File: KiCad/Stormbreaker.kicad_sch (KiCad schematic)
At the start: 42 parts, among them J1 Micro_SD_Card_Det2, J2 USB_C_Receptacle_USB2.0_14P, J3 Conn_01x03, Q1 PMOS, SW1 SW_Push, U1 BQ25895RTW, U3 ATtiny1616-M

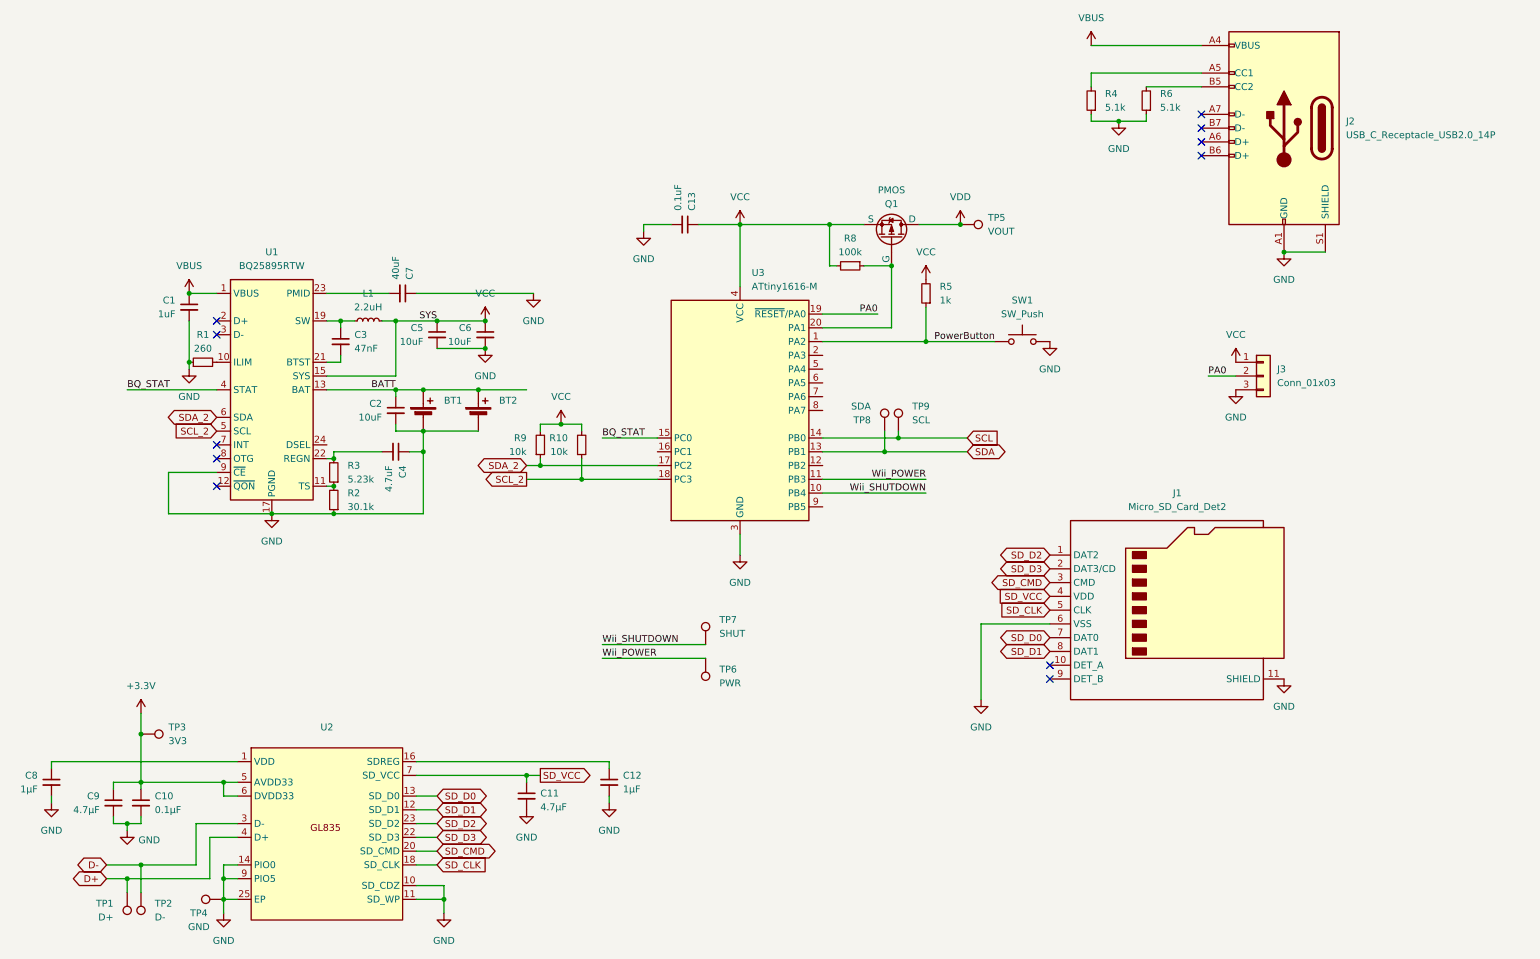
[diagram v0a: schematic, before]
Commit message: Added fan and other batt, via stitched
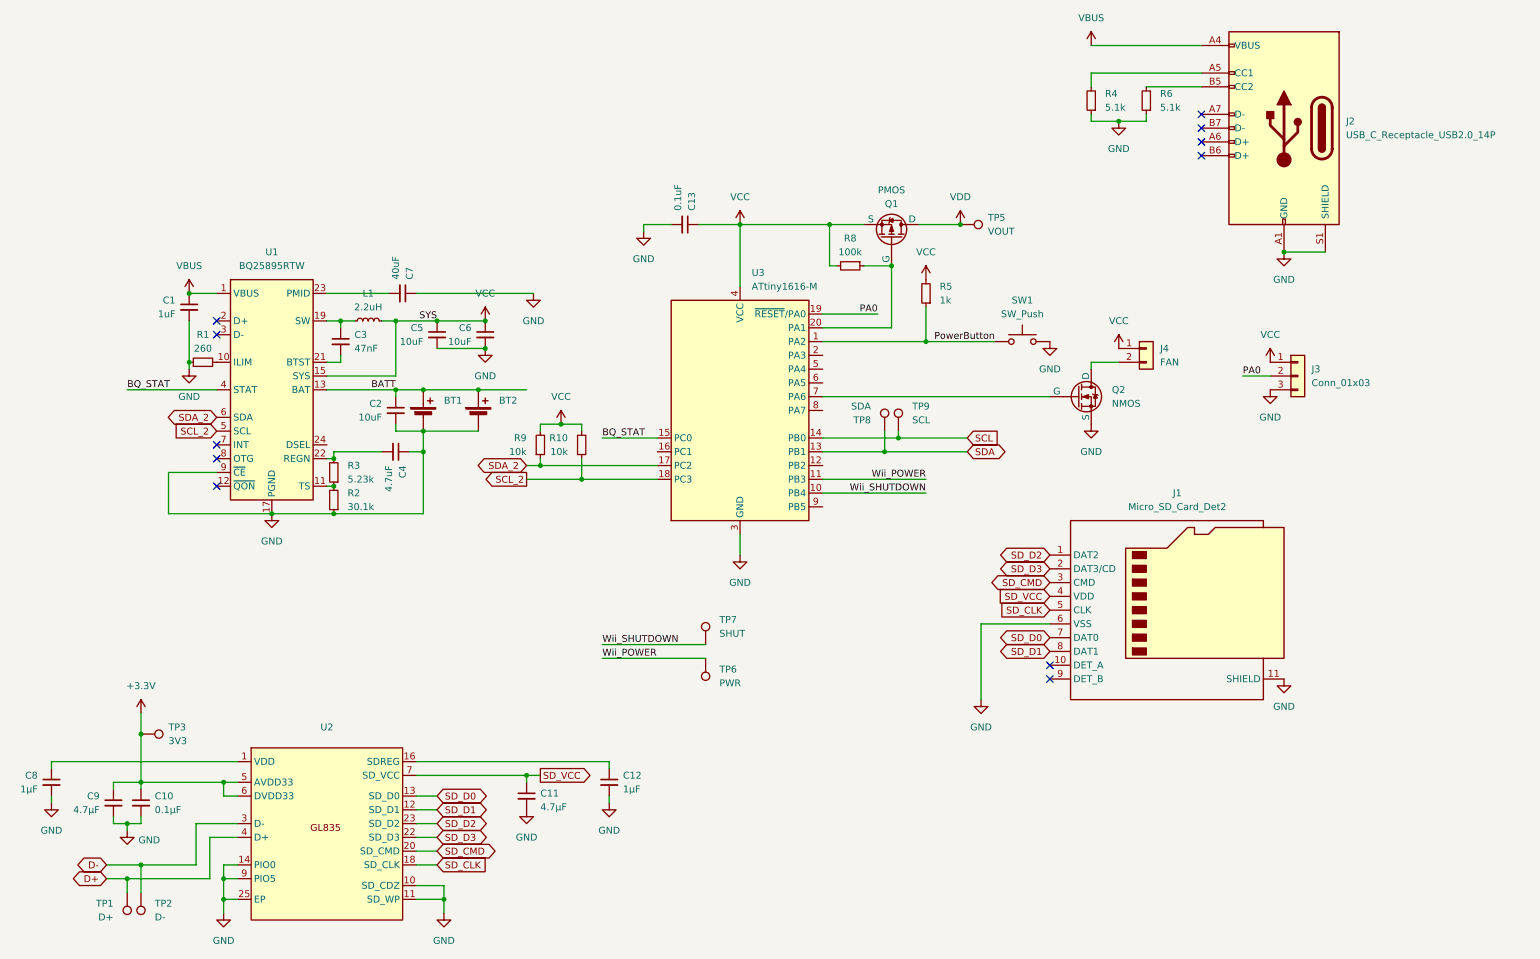
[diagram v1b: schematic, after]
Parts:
- removed TP4: GND, TestPoint:TestPoint_Pad_D3.0mm, symbol Connector:TestPoint
- added J4: FAN, Connector_PinSocket_1.00mm:PinSocket_1x02_P1.00mm_Vertical, symbol Connector_Generic:Conn_01x02
- added Q2: NMOS, Package_TO_SOT_SMD:SOT-23-3, symbol Simulation_SPICE:NMOS
- BT1: footprint Connector_JST:JST_PH_B2B-PH-K_1x02_P2.00mm_Vertical -> Connector_PinSocket_1.27mm:PinSocket_1x02_P1.27mm_Vertical
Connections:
- net GND: now also Q2.2 (S)
- net VCC: now also J4.1 (Pin_1)
- net at U3.7 (PA6): now also Q2.1 (G)
- new net: J4.2 (Pin_2), Q2.3 (D)
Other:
- moved on the sheet: J3

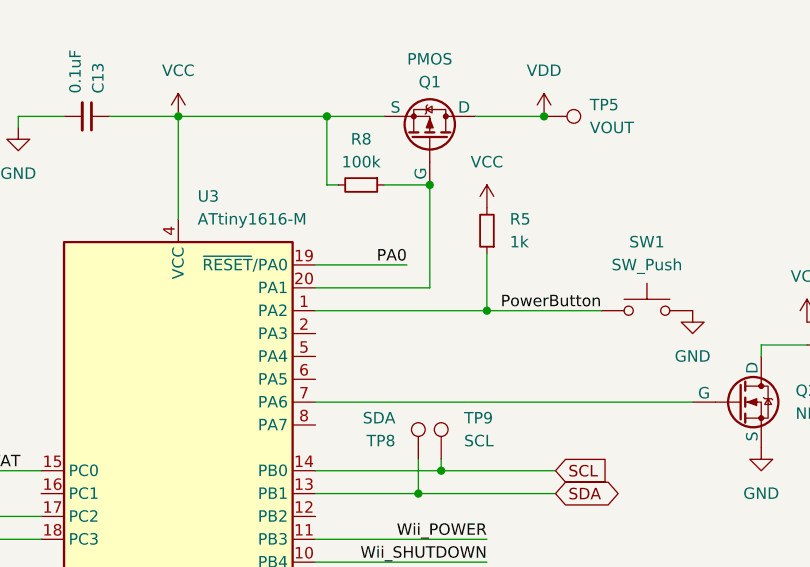
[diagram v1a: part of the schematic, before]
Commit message: Add point for neopixel
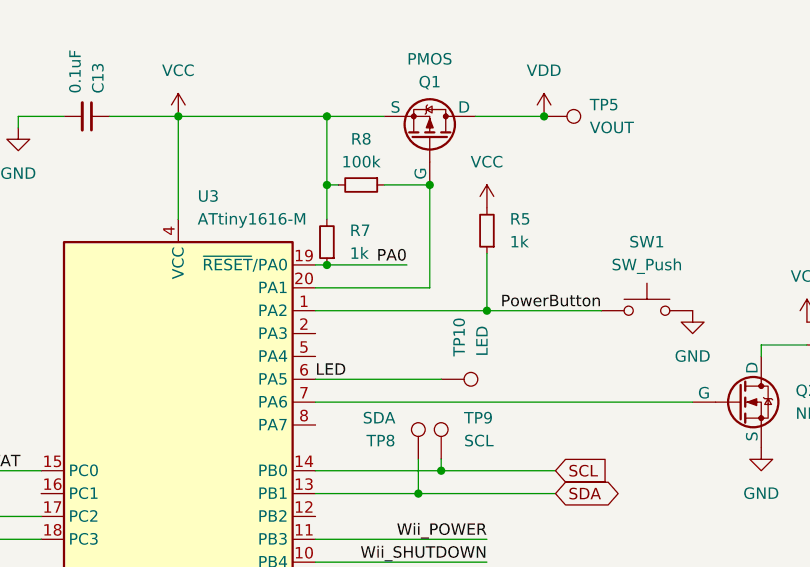
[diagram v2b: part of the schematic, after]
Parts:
- added R7: 1k, Resistor_SMD:R_0603_1608Metric, symbol Device:R_Small
- added TP10: LED, TestPoint:TestPoint_Pad_D1.0mm, symbol Connector:TestPoint
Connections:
- net PA0: now also R7.1
- net VCC: now also R7.2
- net LED: now reaches U3.6 (PA5)
- net LED: now also TP10.1
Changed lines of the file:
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@@
+	)
+	(junction
+		(at 189.23 60.96)
+		(diameter 0)
+		(color 0 0 0 0)
+	)
+	(junction
+		(at 189.23 69.85)
+		(diameter 0)
+		(color 0 0 0 0)
 	)
 	(junction
@@
 	(wire
 		(pts
-			(xy 187.96 69.85) (xy 198.12 69.85)
+			(xy 187.96 69.85) (xy 189.23 69.85)
 		)
 		(stroke
@@
 	(wire
 		(pts
+			(xy 189.23 69.85) (xy 198.12 69.85)
+		)
+		(stroke
+			(width 0)
+			(type default)
+		)
+	)
+	(wire
+		(pts
 			(xy 77.47 171.45) (xy 77.47 173.99)
 		)
@@
 	(wire
 		(pts
+			(xy 189.23 60.96) (xy 189.23 64.77)
+		)
+		(stroke
+			(width 0)
+			(type default)
+		)
+	)
+	(wire
+		(pts
 			(xy 135.89 97.79) (xy 157.48 97.79)
 		)
@@
 	(wire
 		(pts
+			(xy 187.96 82.55) (xy 201.93 82.55)
+		)
+		(stroke
+			(width 0)
+			(type default)
+		)
+	)
+	(wire
+		(pts
 			(xy 59.69 173.99) (xy 74.93 173.99)
 		)
@@
 			(width 0)
 			(type default)
+		)
+	)
+	(label "LED"
+		(at 187.96 82.55 0)
+		(effects
+			(font
+				(size 1.27 1.27)
+			)
+			(justify left bottom)
 		)
 	)
@@
 	)
 	(symbol
+		(lib_id "Device:R_Small")
+		(at 189.23 67.31 180)
+		(unit 1)
+		(exclude_from_sim no)
+		(in_bom yes)
+		(on_board yes)
+		(dnp no)
+		(fields_autoplaced yes)
+		(property "Reference" "R7"
+			(at 191.77 66.0399 0)
+			(effects
+				(font
+					(size 1.27 1.27)
+				)
+				(justify right)
+			)
+		)
+		(property "Value" "1k"
+			(at 191.77 68.5799 0)
+			(effects
+				(font
+					(size 1.27 1.27)
+				)
+				(justify right)
+			)
+		)
+		(property "Footprint" "Resistor_SMD:R_0603_1608Metric"
+			(at 189.23 67.31 0)
+			(effects
+				(font
+					(size 1.27 1.27)
+				)
+				(hide yes)
+			)
+		)
+		(property "Datasheet" "~"
+			(at 189.23 67.31 0)
+			(effects
+				(font
+					(size 1.27 1.27)
+				)
+				(hide yes)
+			)
+		)
+		(property "Description" "Resistor, small symbol"
+			(at 189.23 67.31 0)
+			(effects
+				(font
+					(size 1.27 1.27)
+				)
+				(hide yes)
+			)
+		)
+		(pin "2"
+		)
+		(pin "1"
+		)
+		(instances
+			(project "Stormbreaker"
+				(path "/dcc89f95-4ae4-4756-aa81-33bf4d3c86ca"
+					(reference "R7")
+					(unit 1)
+				)
+			)
+		)
+	)
+	(symbol
 		(lib_id "power:GND")
 		(at 172.72 114.3 0)
@@
 					(unit 1)
 				)
+			)
+		)
+	)
+	(symbol
+		(lib_id "Connector:TestPoint")
+		(at 201.93 82.55 270)
+		(unit 1)
+		(exclude_from_sim no)
+		(in_bom yes)
+		(on_board yes)
+		(dnp no)
+		(property "Reference" "TP10"
+			(at 203.9619 80.01 0)
+			(effects
+				(font
+					(size 1.27 1.27)
+				)
+				(justify right)
+			)
+		)
+		(property "Value" "LED"
+			(at 206.5019 80.01 0)
+			(effects
+				(font
+					(size 1.27 1.27)
+				)
+				(justify right)
+			)
+		)
+		(property "Footprint" "TestPoint:TestPoint_Pad_D1.0mm"
+			(at 201.93 87.63 0)
+			(effects
+				(font
+					(size 1.27 1.27)
+				)
+				(hide yes)
+			)
+		)
+		(property "Datasheet" "~"
+			(at 201.93 87.63 0)
+			(effects
+				(font
+					(size 1.27 1.27)
+				)
+				(hide yes)
+			)
+		)
+		(property "Description" "test point"
+			(at 201.93 82.55 0)
+			(effects
+				(font
+					(size 1.27 1.27)
+				)
+				(hide yes)
+			)
+		)
+		(pin "1"
+		)
+		(instances
+			(project "Stormbreaker"
+				(path "/dcc89f95-4ae4-4756-aa81-33bf4d3c86ca"
+					(reference "TP10")
+					(unit 1)
+				)

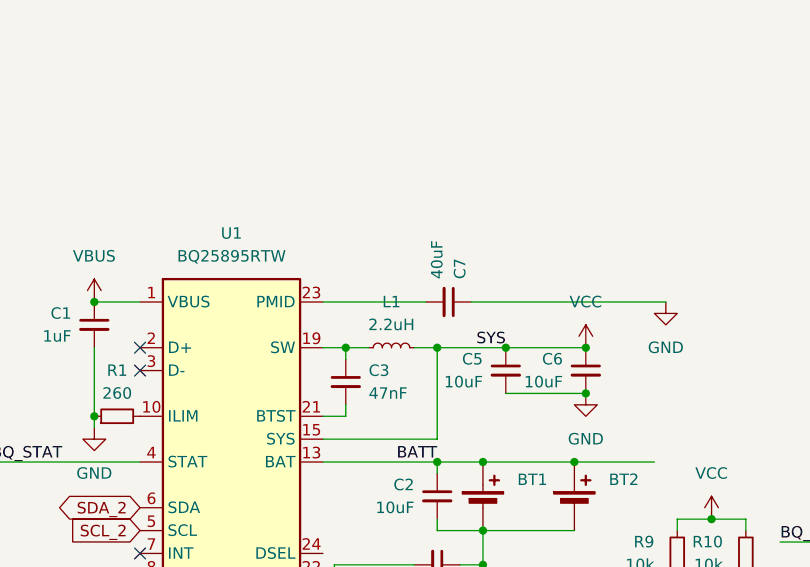
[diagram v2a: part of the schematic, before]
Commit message: Redo power and BQ layout and routing
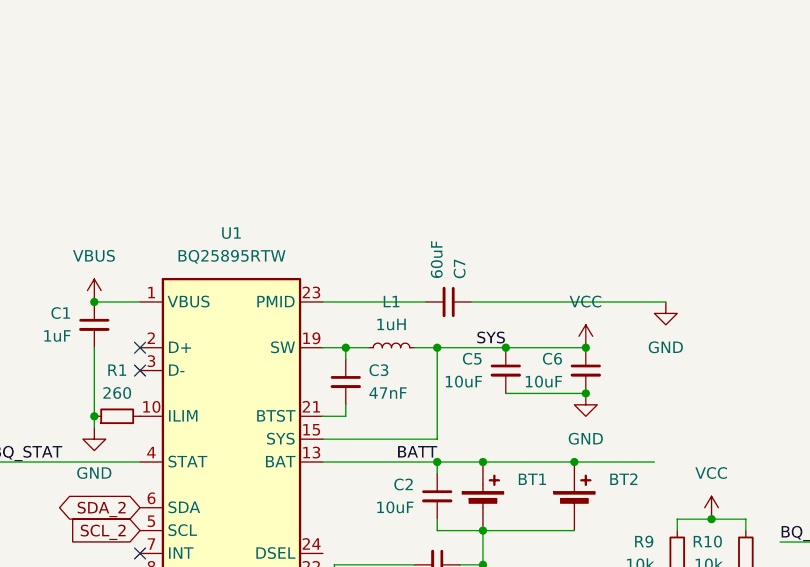
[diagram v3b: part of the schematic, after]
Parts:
- C3, C4: footprint Capacitor_SMD:C_0603_1608Metric -> Capacitor_SMD:C_0402_1005Metric
- C7: value 40uF -> 60uF; footprint Capacitor_SMD:C_0603_1608Metric -> Capacitor_SMD:C_0402_1005Metric
- L1: value 2.2uH -> 1uH; footprint Inductor_SMD:L_Vishay_IHLP-2020 -> Inductor_SMD:L_Taiyo-Yuden_MD-3030; Mouser https://au.mouser.com/ProductDetail/Vishay-Dale/IHLP2020CZE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 -> https://au.mouser.com/ProductDetail/Wurth-Elektronik/784383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; MouserOld (none) -> https://au.mouser.com/ProductDetail/Vishay-Dale/IHLP2020CZE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
- R1, R2, R3: footprint Resistor_SMD:R_0603_1608Metric -> Resistor_SMD:R_0402_1005Metric
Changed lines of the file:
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@@
 			)
 		)
-		(property "Footprint" "Resistor_SMD:R_0603_1608Metric"
+		(property "Footprint" "Resistor_SMD:R_0402_1005Metric"
 			(at 97.79 104.14 0)
 			(effects
@@
 			)
 		)
-		(property "Footprint" "Capacitor_SMD:C_0603_1608Metric"
+		(property "Footprint" "Capacitor_SMD:C_0402_1005Metric"
 			(at 109.22 95.25 0)
 			(effects
@@
 			)
 		)
-		(property "Value" "2.2uH"
+		(property "Value" "1uH"
 			(at 104.14 68.58 90)
 			(effects
@@
 			)
 		)
-		(property "Footprint" "Inductor_SMD:L_Vishay_IHLP-2020"
+		(property "Footprint" "Inductor_SMD:L_Taiyo-Yuden_MD-3030"
 			(at 104.14 71.12 0)
 			(effects
@@
 			)
 		)
-		(property "Mouser" "https://au.mouser.com/ProductDetail/Vishay-Dale/IHLP2020CZER2R2M8A?qs=sGAEpiMZZMv126LJFLh8y6Xt5bZaT3kdfsVdzYQA1S4%3D"
+		(property "MouserOld" "https://au.mouser.com/ProductDetail/Vishay-Dale/IHLP2020CZER2R2M8A?qs=sGAEpiMZZMv126LJFLh8y6Xt5bZaT3kdfsVdzYQA1S4%3D"
+			(at 104.14 71.12 90)
+			(effects
+				(font
+					(size 1.27 1.27)
+				)
+				(hide yes)
+			)
+		)
+		(property "Mouser" "https://au.mouser.com/ProductDetail/Wurth-Elektronik/78438335010HT?qs=a2MtRaTmNOTcep%252BBU0028Q%3D%3D"
 			(at 104.14 71.12 90)
 			(effects
@@
 			)
 		)
-		(property "Footprint" "Resistor_SMD:R_0603_1608Metric"
+		(property "Footprint" "Resistor_SMD:R_0402_1005Metric"
 			(at 73.66 78.74 0)
 			(effects
@@
 			)
 		)
-		(property "Footprint" "Capacitor_SMD:C_0603_1608Metric"
+		(property "Footprint" "Capacitor_SMD:C_0402_1005Metric"
 			(at 99.06 74.93 0)
 			(effects
@@
 			)
 		)
-		(property "Footprint" "Resistor_SMD:R_0603_1608Metric"
+		(property "Footprint" "Resistor_SMD:R_0402_1005Metric"
 			(at 97.79 99.06 0)
 			(effects
@@
 			)
 		)
-		(property "Value" "40uF"
+		(property "Value" "60uF"
 			(at 109.2138 63.5 0)
 			(effects
@@
 			)
 		)
-		(property "Footprint" "Capacitor_SMD:C_0603_1608Metric"
+		(property "Footprint" "Capacitor_SMD:C_0402_1005Metric"
 			(at 110.49 66.04 0)
 			(effects

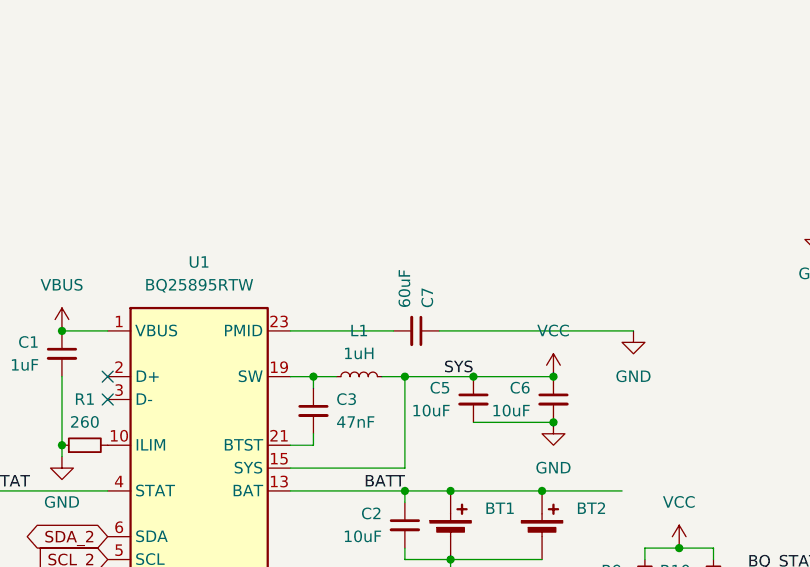
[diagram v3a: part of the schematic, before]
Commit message: Power and ground zones, gnd stitching
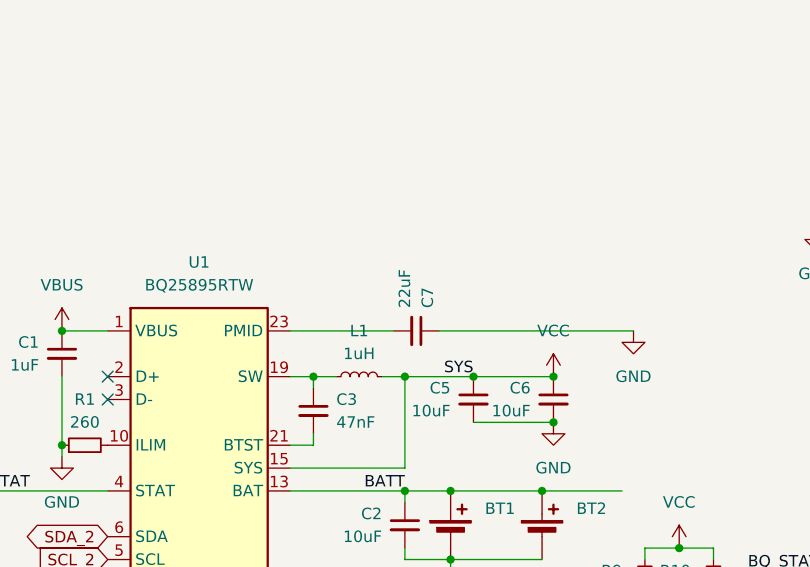
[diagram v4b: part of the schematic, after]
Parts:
- C7: value 60uF -> 22uF
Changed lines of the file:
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@@
 			)
 		)
-		(property "Value" "60uF"
+		(property "Value" "22uF"
 			(at 109.2138 63.5 0)
 			(effects
